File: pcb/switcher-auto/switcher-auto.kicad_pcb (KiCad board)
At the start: 4 copper layers, 100 x 138 mm, 42 parts, among them J1 MD-90SM, J10 MD-90SM, J11 MD-90SM, J12 MD-90SM, J13 MD-90SM, J14 MD-90SM, J15 Conn_02x22_Top_Bottom, J2 Conn_02x22_Top_Bottom, J3 Conn_02x22_Top_Bottom, J4 Conn_02x22_Top_Bottom, SW1 SW_Push, SW2 SW_Push, U1 CD74HC4067SM96, U2 CD74HC4067SM96, U3 CD74HC4067SM96, U4 CD74HC4067SM96, U5 CD74HC4067SM96, U6 CD74HC4067SM96, U7 CD74HC4067SM96

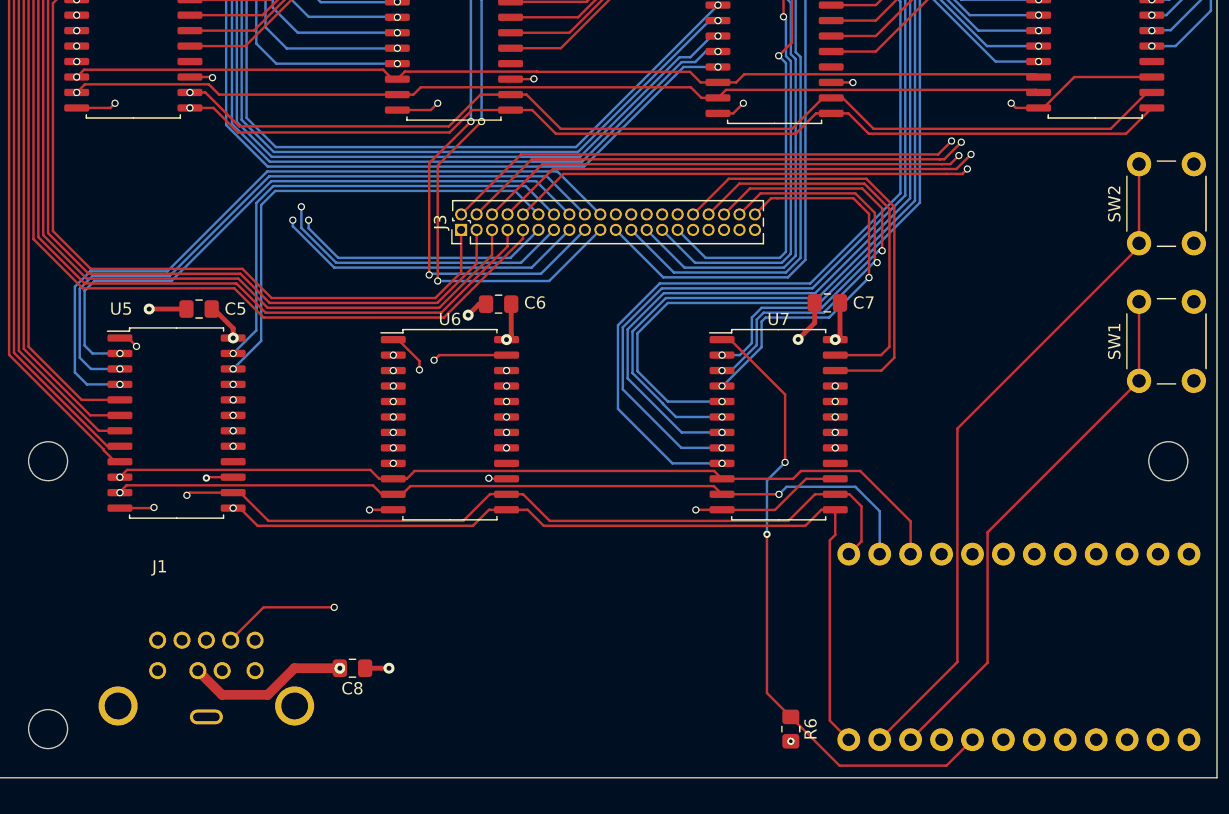
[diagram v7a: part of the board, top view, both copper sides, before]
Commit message: Hooks up V sense muxer
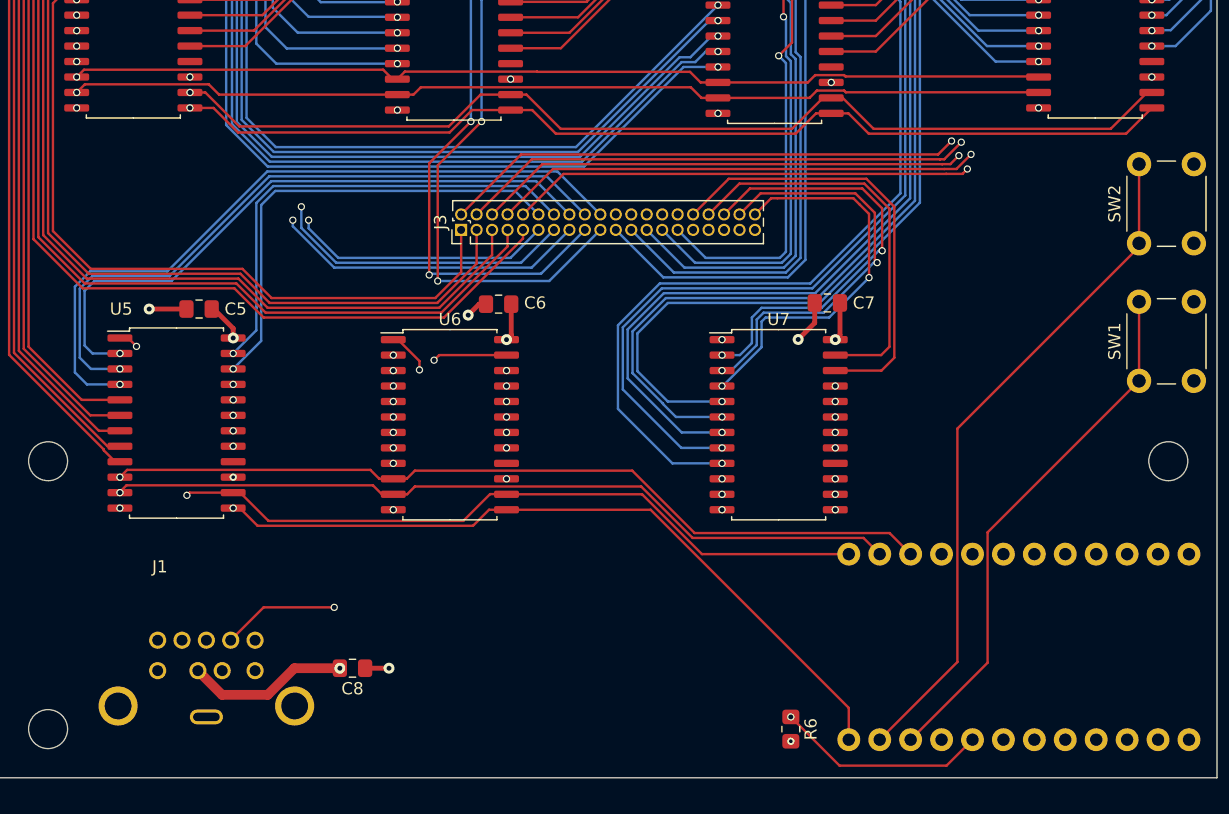
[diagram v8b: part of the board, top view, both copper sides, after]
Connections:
- U7 pad 10: /S0 -> /R0
- U7 pad 11: /S1 -> /R1
- U7 pad 13: /S3 -> /R3
- U7 pad 14: /S2 -> /R2
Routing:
- net GND: track 77.6 -> 28.9 mm, vias 20 -> 22
- net /R1: track 0.00 -> 32.0 mm, vias 0 -> 1
- net /R0: track 0.00 -> 29.8 mm, vias 0 -> 1
- net /R3: track 0.00 -> 19.6 mm, vias 0 -> 1
- net /R2: track 0.00 -> 14.8 mm, vias 0 -> 1
- net /S3: track 191.3 -> 181.0 mm
- net /S2: track 185.0 -> 179.4 mm
- net /S1: track 183.1 -> 180.5 mm, vias 3 -> 2
- net /S0: track 185.6 -> 183.5 mm
